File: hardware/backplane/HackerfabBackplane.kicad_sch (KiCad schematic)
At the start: 7 parts, among them J1 9001-12961C00A, J2 9001-12961C00A, J3 9001-12961C00A

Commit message: Update backplane and libraries from October 26 archives
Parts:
- added J4, J5, J6: KF128-5.08-2P-AA, Hack_Connector:KF128-5.08-2P-AA, symbol Hack_Connector:KF128-5.08-2P-AA
- added J7: TYPE-C-31-M-12, Hack_Connector:USB_C_Receptacle_HRO_TYPE-C-31-M-12, symbol Hack_Connector:TYPE-C-31-M-12
- added J9: ZX-SH1.0-3PWT, Hack_Connector:Megastar_ZX-SH1.0-3PWT_1x03_P1.00mm_Horizontal, symbol Hack_Connector:ZX-SH1.0-3PWT
- added R22, R23: 5k1, Resistor_SMD:R_0603_1608Metric, symbol Hack_Passives:RMEF0603JT5K10
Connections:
- net +12V: now also J5.1
- net +24V: now also J4.1; no longer J1.A1, J1.A2, J1.A31, J1.A32, J1.C1, J1.C2, J1.C31, J1.C32, J2.A1, J2.A2, J2.A31, J2.A32, J2.C1, J2.C2, J2.C31, J2.C32, J3.A1, J3.A2, J3.A31, J3.A32, J3.C1, J3.C2, J3.C31, J3.C32
- net +5V: now also J6.1
- net GND: now also J4.2, J5.2, J6.2, J7.A1 (GND), J7.A12 (GND), J7.B1 (GND), J7.B12 (GND), J7.SH (SHIELD), J9.2 (GND), R22.2, R23.2
- new net: J7.A5 (CC1), R23.1
- new net: J7.B5 (CC2), R22.1
- new net +24V_P: J1.A1, J1.A2, J1.A31, J1.A32, J1.C1, J1.C2, J1.C31, J1.C32, J2.A1, J2.A2, J2.A31, J2.A32, J2.C1, J2.C2, J2.C31, J2.C32, J3.A1, J3.A2, J3.A31, J3.A32, J3.C1, J3.C2, J3.C31, J3.C32
- new net +5V_USB: J7.A4 (VBUS), J7.A9 (VBUS), J7.B4 (VBUS), J7.B9 (VBUS)
- new net SWCLK: J9.1 (SWCLK)
- new net SWDIO: J9.3 (SWDIO)
- new net USB_D+: J7.A6 (D+), J7.B6 (D+)
- new net USB_D-: J7.A7 (D-), J7.B7 (D-)
- no-connect marks 23 -> 25
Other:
- added sheet Protection (Protection.kicad_sch)
- note removed: "Add USB-C"
- note removed: "Add fuse circuit"
- note removed: "Add main power+secondary power connectors"
- moved on the sheet: H1, H2, H3, H4

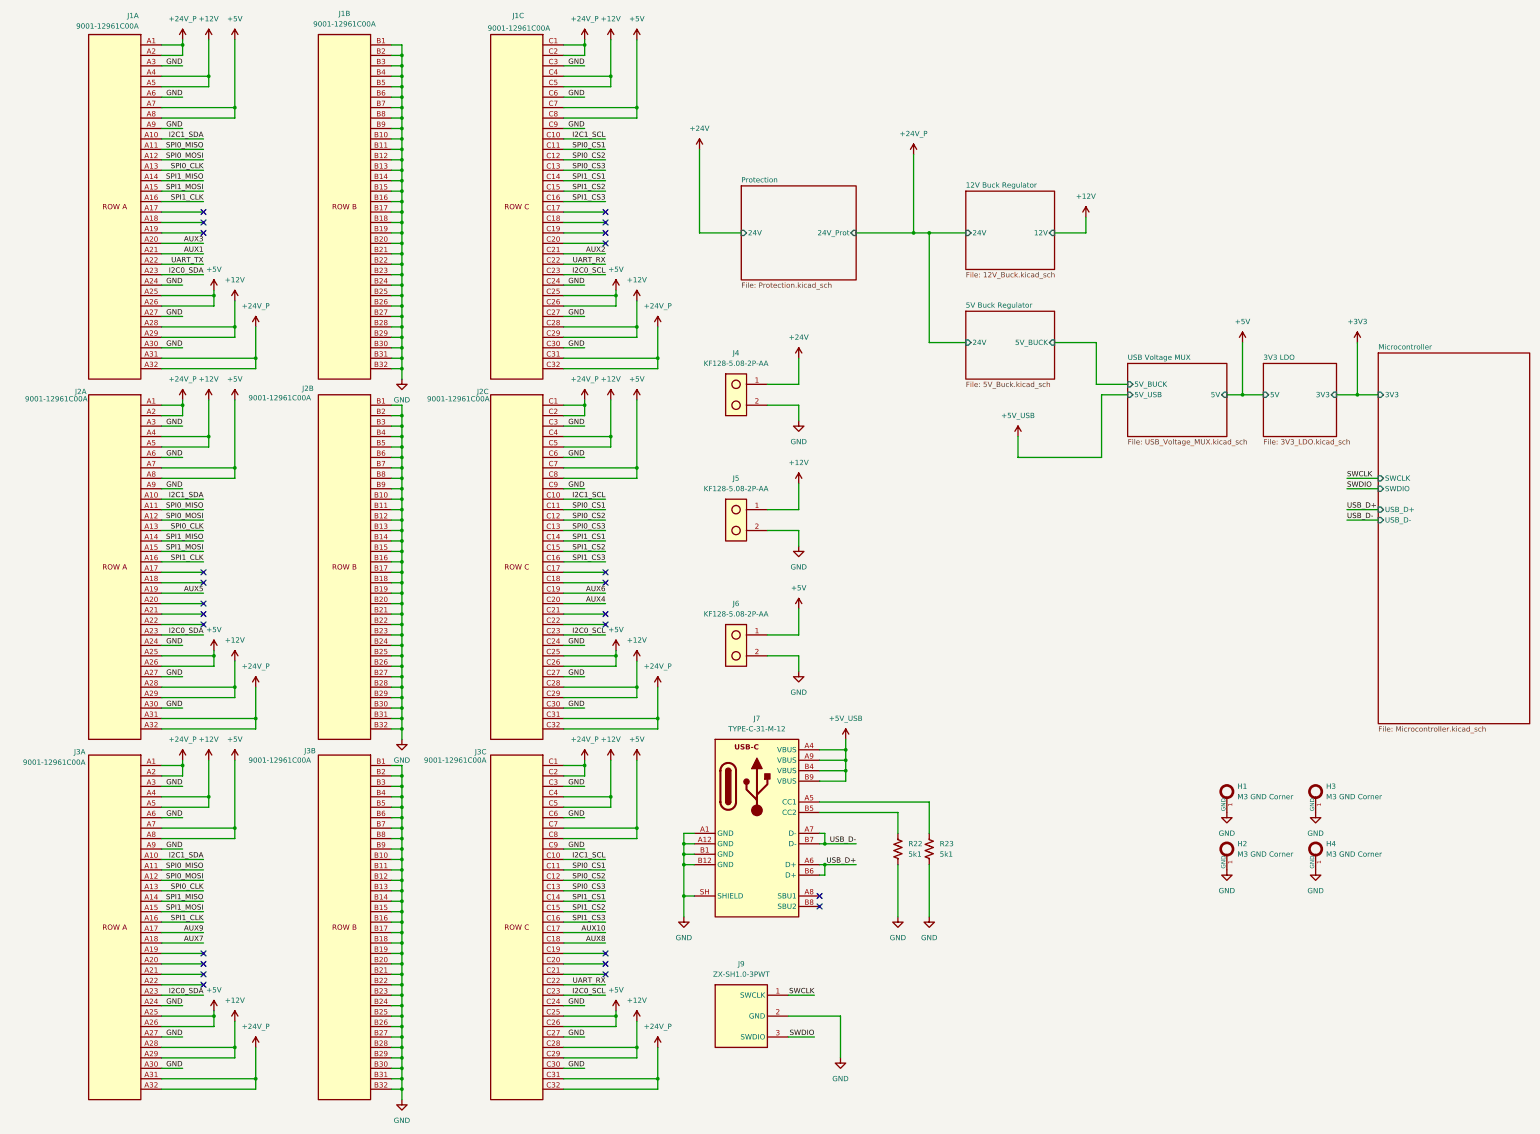
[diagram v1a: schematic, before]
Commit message: Update backplane and libraries from October 29 archives
Import the supplied active KiCad sources, retain portable library tables, and omit local editor state. Refresh schematic and board previews, archive fingerprints, and validation notes for the partially routed 144-component design.
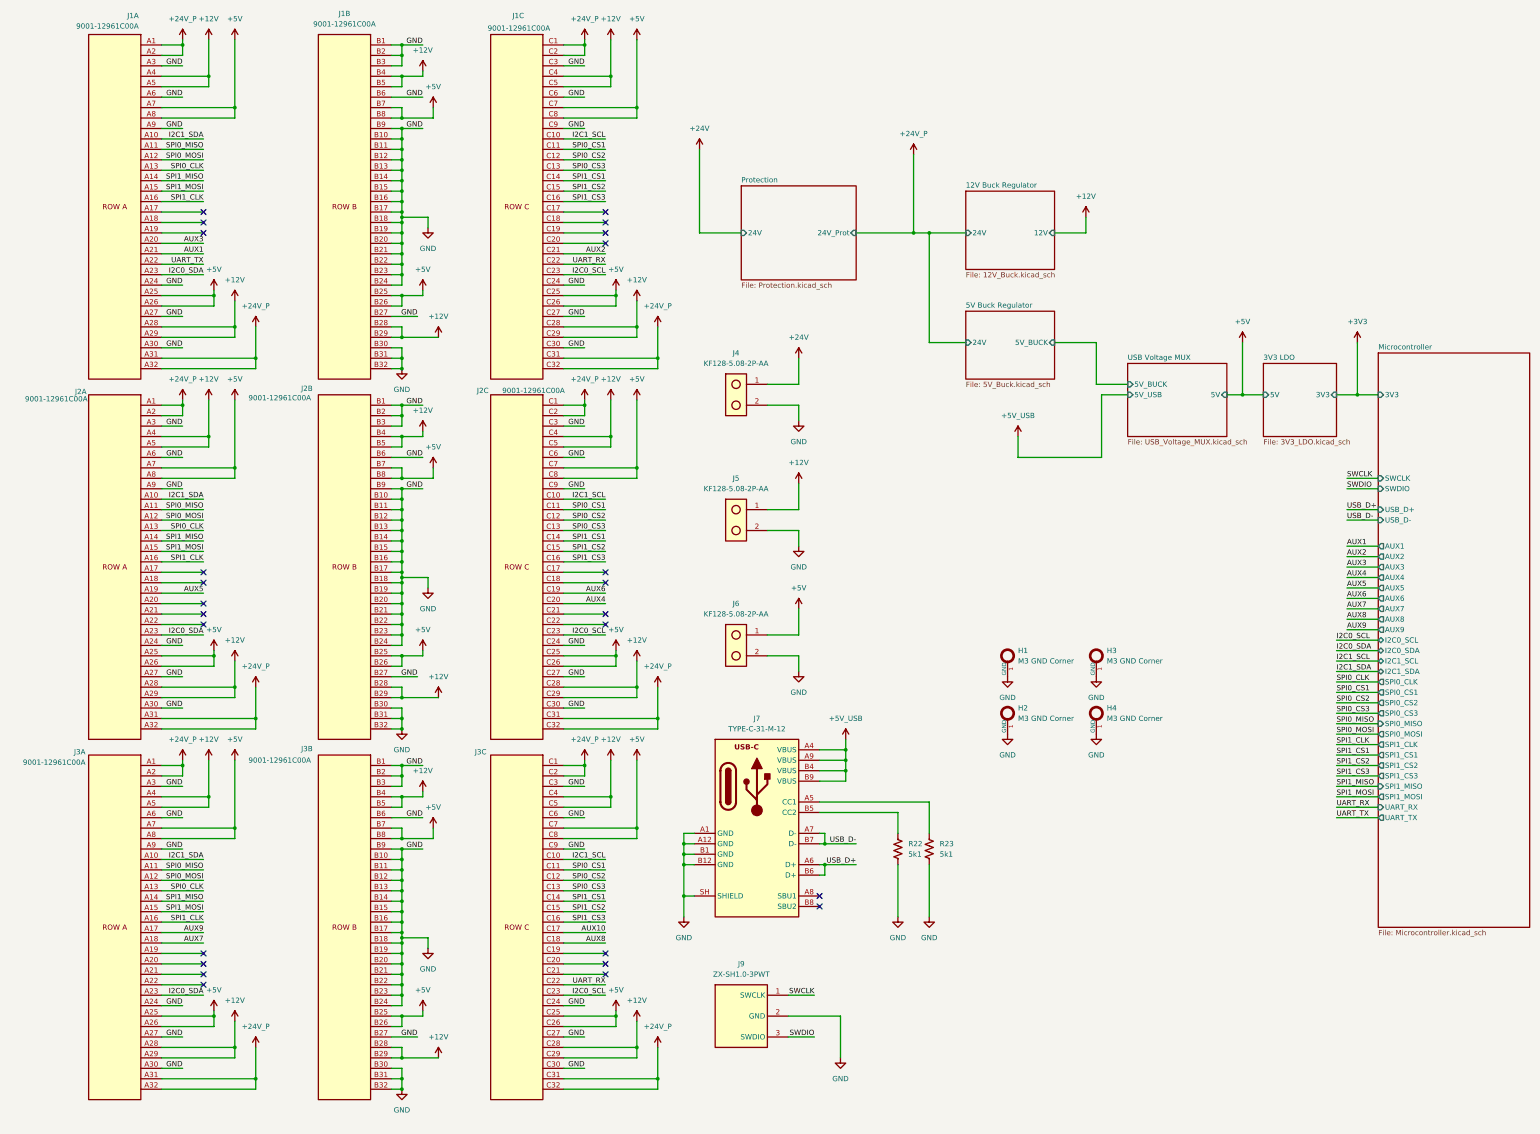
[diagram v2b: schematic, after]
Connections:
- net +12V: now also J1.B28, J1.B29, J1.B4, J1.B5, J2.B28, J2.B29, J2.B4, J2.B5, J3.B28, J3.B29, J3.B4, J3.B5
- net +5V: now also J1.B25, J1.B26, J1.B7, J1.B8, J2.B25, J2.B26, J2.B7, J2.B8, J3.B25, J3.B26, J3.B7, J3.B8
- net GND: no longer J1.B25, J1.B26, J1.B28, J1.B29, J1.B4, J1.B5, J1.B7, J1.B8, J2.B25, J2.B26, J2.B28, J2.B29, J2.B4, J2.B5, J2.B7, J2.B8, J3.B25, J3.B26, J3.B28, J3.B29, J3.B4, J3.B5, J3.B7, J3.B8
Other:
- sheet Microcontroller ports: added AUX1, AUX2, AUX3, AUX4, AUX5, AUX6, AUX7, AUX8, AUX9, I2C0_SCL, I2C0_SDA, I2C1_SCL, I2C1_SDA, SPI0_CLK, SPI0_CS1, SPI0_CS2, SPI0_CS3, SPI0_MISO, SPI0_MOSI, SPI1_CLK, SPI1_CS1, SPI1_CS2, SPI1_CS3, SPI1_MISO, SPI1_MOSI, UART_RX, UART_TX; removed none
- moved on the sheet: H1, H2, H3, H4

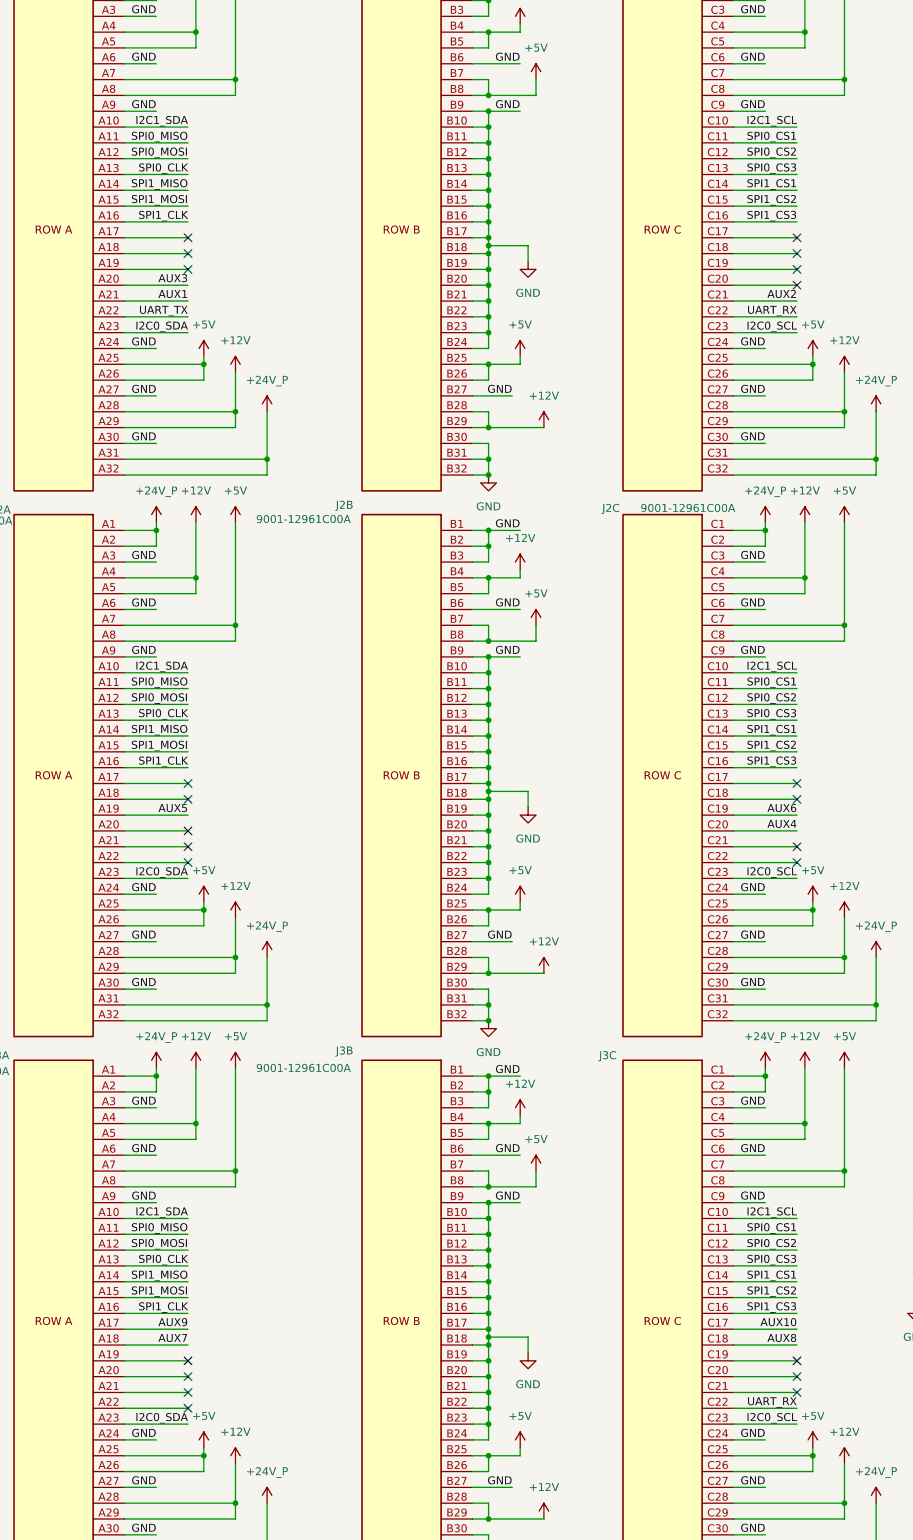
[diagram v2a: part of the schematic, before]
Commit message: Arrange connector signals around the MCU jumper banks
Keep each protocol paired across A/C columns and UART RX/TX together. Update schematic and PCB signal assignments, add pin tables and a top-layer passage guide, and verify fixed power/ground, signal inventory, source jumpers, and KiCad parity.
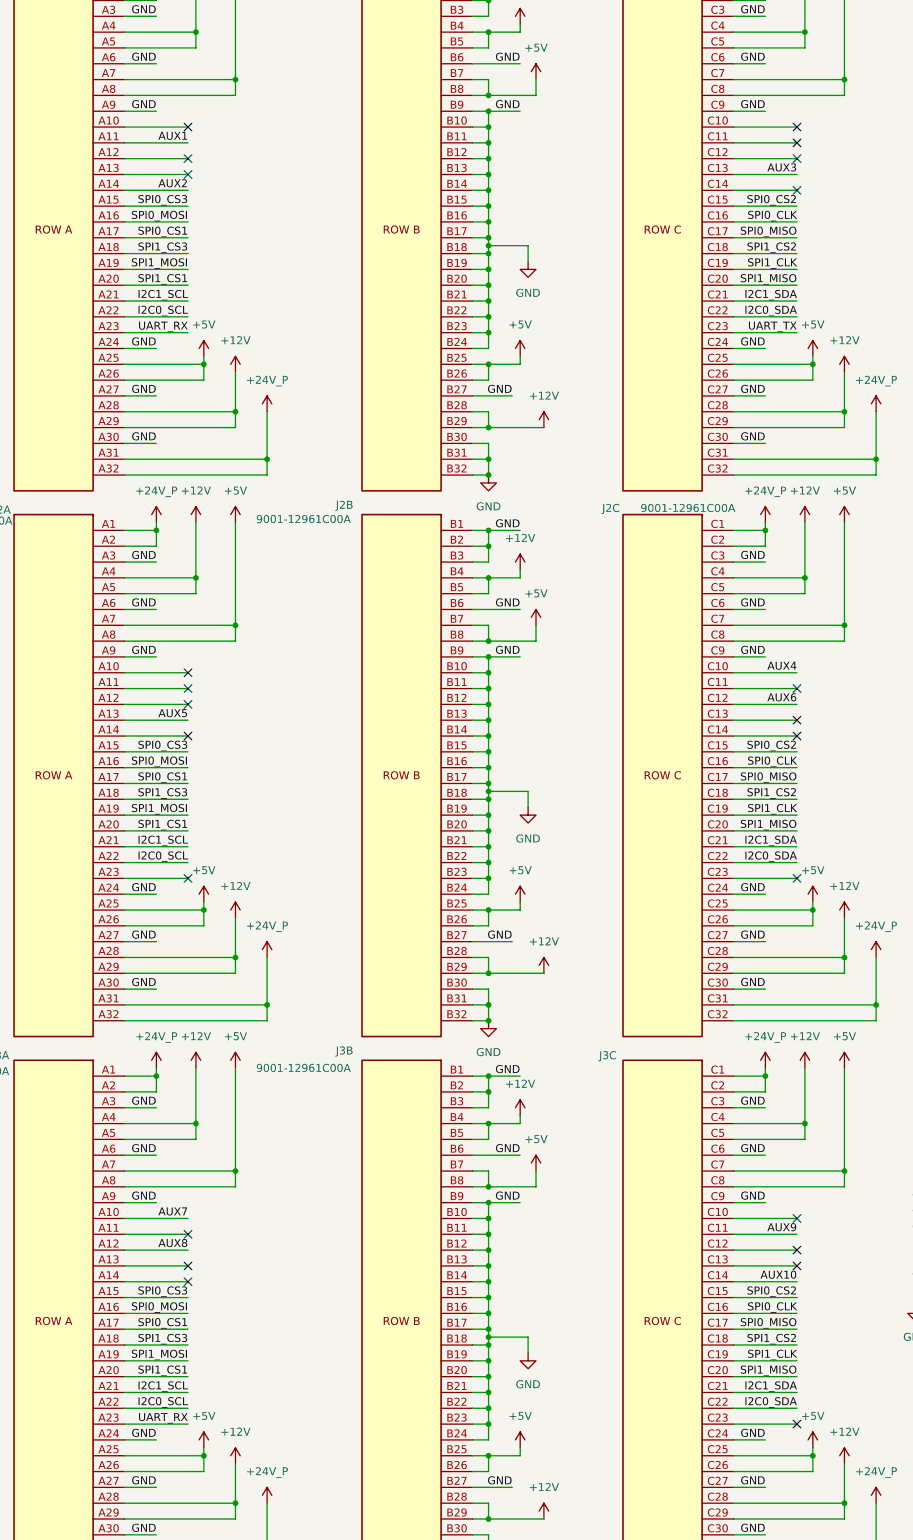
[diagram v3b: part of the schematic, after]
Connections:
- net AUX1: now also J1.A11; no longer J1.A21
- net AUX10: now also J3.C14; no longer J3.C17
- net AUX2: now also J1.A14; no longer J1.C21
- net AUX3: now also J1.C13; no longer J1.A20
- net AUX4: now also J2.C10; no longer J2.C20
- net AUX5: now also J2.A13; no longer J2.A19
- net AUX6: now also J2.C12; no longer J2.C19
- net AUX7: now also J3.A10; no longer J3.A18
- net AUX8: now also J3.A12; no longer J3.C18
- net AUX9: now also J3.C11; no longer J3.A17
- net I2C0_SCL: now also J1.A22, J2.A22, J3.A22; no longer J1.C23, J2.C23, J3.C23
- net I2C0_SDA: now also J1.C22, J2.C22, J3.C22; no longer J1.A23, J2.A23, J3.A23
- net I2C1_SCL: now also J1.A21, J2.A21, J3.A21; no longer J1.C10, J2.C10, J3.C10
- net I2C1_SDA: now also J1.C21, J2.C21, J3.C21; no longer J1.A10, J2.A10, J3.A10
- net SPI0_CLK: now also J1.C16, J2.C16, J3.C16; no longer J1.A13, J2.A13, J3.A13
- net SPI0_CS1: now also J1.A17, J2.A17, J3.A17; no longer J1.C11, J2.C11, J3.C11
- net SPI0_CS2: now also J1.C15, J2.C15, J3.C15; no longer J1.C12, J2.C12, J3.C12
- net SPI0_CS3: now also J1.A15, J2.A15, J3.A15; no longer J1.C13, J2.C13, J3.C13
- net SPI0_MISO: now also J1.C17, J2.C17, J3.C17; no longer J1.A11, J2.A11, J3.A11
- net SPI0_MOSI: now also J1.A16, J2.A16, J3.A16; no longer J1.A12, J2.A12, J3.A12
- net SPI1_CLK: now also J1.C19, J2.C19, J3.C19; no longer J1.A16, J2.A16, J3.A16
- net SPI1_CS1: now also J1.A20, J2.A20, J3.A20; no longer J1.C14, J2.C14, J3.C14
- net SPI1_CS2: now also J1.C18, J2.C18, J3.C18; no longer J1.C15, J2.C15, J3.C15
- net SPI1_CS3: now also J1.A18, J2.A18, J3.A18; no longer J1.C16, J2.C16, J3.C16
- net SPI1_MISO: now also J1.C20, J2.C20, J3.C20; no longer J1.A14, J2.A14, J3.A14
- net SPI1_MOSI: now also J1.A19, J2.A19, J3.A19; no longer J1.A15, J2.A15, J3.A15
- net UART_RX: now also J1.A23, J3.A23; no longer J1.C22, J3.C22
- net UART_TX: now also J1.C23; no longer J1.A22

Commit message: Import October 30 V6 schematic and routing updates
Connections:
- net AUX1: now also J1.A14; no longer J1.A11
- net AUX10: now also J3.C19; no longer J3.C14
- net AUX2: now also J1.A19; no longer J1.A14
- net AUX3: now also J1.C18; no longer J1.C13
- net AUX4: now also J2.C13; no longer J2.C10
- net AUX5: now also J2.A18; no longer J2.A13
- net AUX6: now also J2.C15; no longer J2.C12
- net AUX7: now also J3.A13; no longer J3.A10
- net AUX8: now also J3.A15; no longer J3.A12
- net AUX9: now also J3.C14; no longer J3.C11
- net I2C0_SCL: now also J1.A16, J2.A16, J3.A16; no longer J1.A22, J2.A22, J3.A22
- net I2C0_SDA: now also J1.C16, J2.C16, J3.C16; no longer J1.C22, J2.C22, J3.C22
- net I2C1_SCL: now also J1.A17, J2.A17, J3.A17; no longer J1.A21, J2.A21, J3.A21
- net I2C1_SDA: now also J1.C17, J2.C17, J3.C17; no longer J1.C21, J2.C21, J3.C21
- net SPI0_CLK: now also J1.C11, J2.C11, J3.C11; no longer J1.C16, J2.C16, J3.C16
- net SPI0_CS1: now also J1.A12, J2.A12, J3.A12; no longer J1.A17, J2.A17, J3.A17
- net SPI0_CS2: now also J1.C10, J2.C10, J3.C10; no longer J1.C15, J2.C15, J3.C15
- net SPI0_CS3: now also J1.A10, J2.A10, J3.A10; no longer J1.A15, J2.A15, J3.A15
- net SPI0_MISO: now also J1.C12, J2.C12, J3.C12; no longer J1.C17, J2.C17, J3.C17
- net SPI0_MOSI: now also J1.A11, J2.A11, J3.A11; no longer J1.A16, J2.A16, J3.A16
- net SPI1_CLK: now also J1.C22, J2.C22, J3.C22; no longer J1.C19, J2.C19, J3.C19
- net SPI1_CS1: now also J1.A23, J2.A23, J3.A23; no longer J1.A20, J2.A20, J3.A20
- net SPI1_CS2: now also J1.C21, J2.C21, J3.C21; no longer J1.C18, J2.C18, J3.C18
- net SPI1_CS3: now also J1.A21, J2.A21, J3.A21; no longer J1.A18, J2.A18, J3.A18
- net SPI1_MISO: now also J1.C23, J2.C23, J3.C23; no longer J1.C20, J2.C20, J3.C20
- net SPI1_MOSI: now also J1.A22, J2.A22, J3.A22; no longer J1.A19, J2.A19, J3.A19
- net UART_RX: now also J1.A20; no longer J1.A23, J3.A23
- net UART_TX: now also J1.C20; no longer J1.C23
- no-connect marks 25 -> 26
